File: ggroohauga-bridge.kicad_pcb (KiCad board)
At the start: 2 copper layers, 98.5 x 31 mm, 12 parts

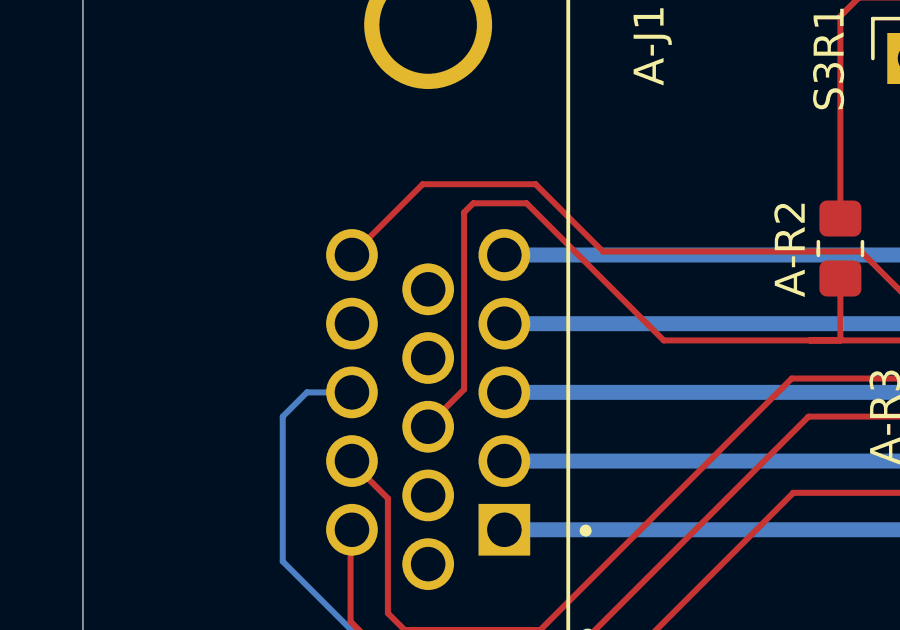
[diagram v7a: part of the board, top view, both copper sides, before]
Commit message: Add 3D models of the DE-15 connectors and realign some tracks
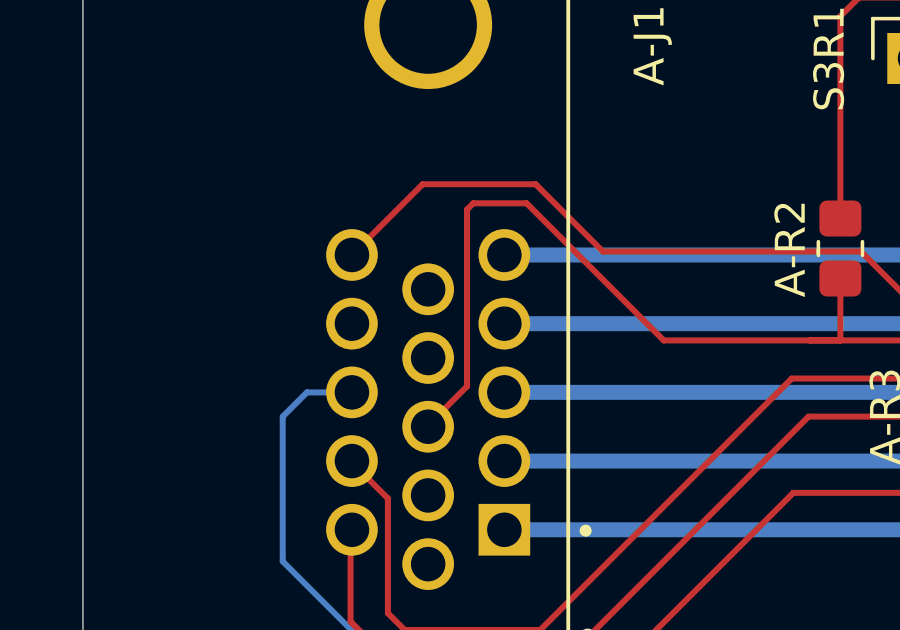
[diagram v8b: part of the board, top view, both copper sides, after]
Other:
- board text added: "urn:oid:1.3.6.1.4.1.39777.1.3.1.3.4"
- board text removed: "urn:oid:1.3.6.1.4.1.39777.1.3.1.3.3"
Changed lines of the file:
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@@
 		(0 "F.Cu" signal)
 		(2 "B.Cu" signal)
-		(9 "F.Adhes" user "F.Adhesive")
-		(11 "B.Adhes" user "B.Adhesive")
 		(13 "F.Paste" user)
 		(15 "B.Paste" user)
@@
 		(17 "Dwgs.User" user "User.Drawings")
 		(19 "Cmts.User" user "User.Comments")
-		(21 "Eco1.User" user "User.Eco1")
-		(23 "Eco2.User" user "User.Eco2")
 		(25 "Edge.Cuts" user)
 		(27 "Margin" user)
@@
 		(35 "F.Fab" user)
 		(33 "B.Fab" user)
-		(39 "User.1" user)
-		(41 "User.2" user)
-		(43 "User.3" user)
-		(45 "User.4" user)
-		(47 "User.5" user)
-		(49 "User.6" user)
-		(51 "User.7" user)
-		(53 "User.8" user)
-		(55 "User.9" user)
 	)
 	(setup
@@
 		)
 		(embedded_fonts no)
+		(model "${KIPRJMOD}/vendor/amphenol/L77HDE15SD1CH4R.step"
+			(offset
+				(xyz 0 0 0)
+			)
+			(scale
+				(xyz 1 1 1)
+			)
+			(rotate
+				(xyz -90 -0 -0)
+			)
+		)
 	)
 	(footprint "LOGO"
@@
 		(fp_line
 			(start -15.405 4.67)
-			(end -15.405 -11.43)
+			(end 15.405 4.67)
 			(stroke
 				(width 0.127)
@@
 		)
 		(fp_line
-			(start 15.405 4.67)
+			(start -15.405 -11.43)
 			(end -15.405 4.67)
 			(stroke
@@
 		)
 		(fp_line
-			(start 15.405 4.67)
-			(end 15.405 -11.43)
+			(start 15.405 -11.43)
+			(end 15.405 4.67)
 			(stroke
 				(width 0.127)
@@
 		(fp_line
 			(start -15.655 4.92)
-			(end 15.655 4.92)
+			(end -15.655 -17.68)
 			(stroke
 				(width 0.05)
@@
 		(fp_line
 			(start 15.655 4.92)
-			(end 15.655 -17.68)
+			(end -15.655 4.92)
 			(stroke
 				(width 0.05)
@@
 		(fp_line
 			(start -15.655 -17.68)
-			(end -15.655 4.92)
+			(end 15.655 -17.68)
 			(stroke
 				(width 0.05)
@@
 		(fp_line
 			(start 15.655 -17.68)
-			(end -15.655 -17.68)
+			(end 15.655 4.92)
 			(stroke
 				(width 0.05)
@@
 		(fp_line
 			(start -15.405 4.67)
-			(end -15.405 -11.43)
+			(end 15.405 4.67)
 			(stroke
 				(width 0.127)
@@
 		)
 		(fp_line
-			(start 15.405 4.67)
+			(start -15.405 -11.43)
 			(end -15.405 4.67)
 			(stroke
@@
 		)
 		(fp_line
-			(start 15.405 4.67)
-			(end 15.405 -17.43)
+			(start -15.405 -11.43)
+			(end 22.86 -11.43)
 			(stroke
 				(width 0.127)
@@
 		)
 		(fp_line
-			(start -15.405 -11.43)
-			(end -15.405 -17.43)
+			(start -15.405 -17.43)
+			(end -15.405 -11.43)
 			(stroke
 				(width 0.127)
@@
 		)
 		(fp_line
-			(start 22.86 -11.43)
-			(end -15.405 -11.43)
+			(start -15.405 -17.43)
+			(end 15.405 -17.43)
 			(stroke
 				(width 0.127)
@@
 		(fp_line
 			(start 15.405 -17.43)
-			(end -15.405 -17.43)
+			(end 15.405 4.67)
 			(stroke
 				(width 0.127)
@@
 		)
 		(embedded_fonts no)
+		(model "${KIPRJMOD}/vendor/amphenol/L717HDE15PD1CH4F.step"
+			(offset
+				(xyz 0 -8.5 6.25)
+			)
+			(scale
+				(xyz 1 1 1)
+			)
+			(rotate
+				(xyz -180 -0 -0)
+			)
+		)
 	)
 	(gr_rect
@@
 		)
 	)
-	(gr_text "urn:oid:1.3.6.1.4.1.39777.1.3.1.3.3"
+	(gr_text "urn:oid:1.3.6.1.4.1.39777.1.3.1.3.4"
 		(at 131.064 56.642 0)
 		(layer "B.SilkS")
@@
 	)
 	(segment
-		(start 78.105 64.008)
-		(end 73.2326 64.008)
+		(start 66.8826 59.436)
+		(end 66.675 59.6436)
 		(width 0.2)
 		(layer "F.Cu")
@@
 	)
 	(segment
-		(start 79.105 63.992)
-		(end 79.121 64.008)
+		(start 66.675 65.542)
+		(end 65.3328 66.8842)
 		(width 0.2)
 		(layer "F.Cu")
@@
 	)
 	(segment
-		(start 89.33 64.008)
-		(end 78.105 64.008)
+		(start 68.6606 59.436)
+		(end 66.8826 59.436)
 		(width 0.2)
 		(layer "F.Cu")
@@
 	)
 	(segment
-		(start 73.2326 64.008)
-		(end 68.6606 59.436)
+		(start 79.105 63.992)
+		(end 79.121 64.008)
 		(width 0.2)
 		(layer "F.Cu")
@@
 	)
 	(segment
-		(start 79.121 61.944)
-		(end 79.121 63.976)
+		(start 89.33 64.008)
+		(end 78.105 64.008)
 		(width 0.2)
 		(layer "F.Cu")
@@
 	)
 	(segment
-		(start 79.121 64.008)
-		(end 78.105 64.008)
+		(start 66.675 59.6436)
+		(end 66.675 65.542)
 		(width 0.2)
 		(layer "F.Cu")
@@
 	)
 	(segment
-		(start 66.5778 59.7408)
-		(end 66.5778 65.6392)
+		(start 79.121 61.944)
+		(end 79.121 63.976)
 		(width 0.2)
 		(layer "F.Cu")
@@
 	)
 	(segment
-		(start 68.6606 59.436)
-		(end 66.8826 59.436)
+		(start 79.121 64.008)
+		(end 78.105 64.008)
 		(width 0.2)
 		(layer "F.Cu")
@@
 	)
 	(segment
-		(start 66.5778 65.6392)
-		(end 65.3328 66.8842)
+		(start 78.105 64.008)
+		(end 73.2326 64.008)
 		(width 0.2)
 		(layer "F.Cu")
@@
 	)
 	(segment
-		(start 66.8826 59.436)
-		(end 66.5778 59.7408)
+		(start 73.2326 64.008)
+		(end 68.6606 59.436)
 		(width 0.2)
 		(layer "F.Cu")
